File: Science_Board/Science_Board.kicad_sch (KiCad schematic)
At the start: 26 parts, among them J1 Conn_01x02, J10 Conn_01x02, J11 Conn_01x03, J12 Conn_01x03, J13 Conn_01x03, J14 Conn_01x03, J15 Conn_01x03, J16 Conn_01x03, J17 Conn_01x03, J18 Conn_01x03, J19 Conn_01x02, J2 Conn_01x02, J20 Molex_Megafit_02, J5 Conn_01x02, J6 Conn_01x04, J7 Conn_01x03, J8 Conn_01x03, J9 Conn_01x02, U5 PCA9685BS

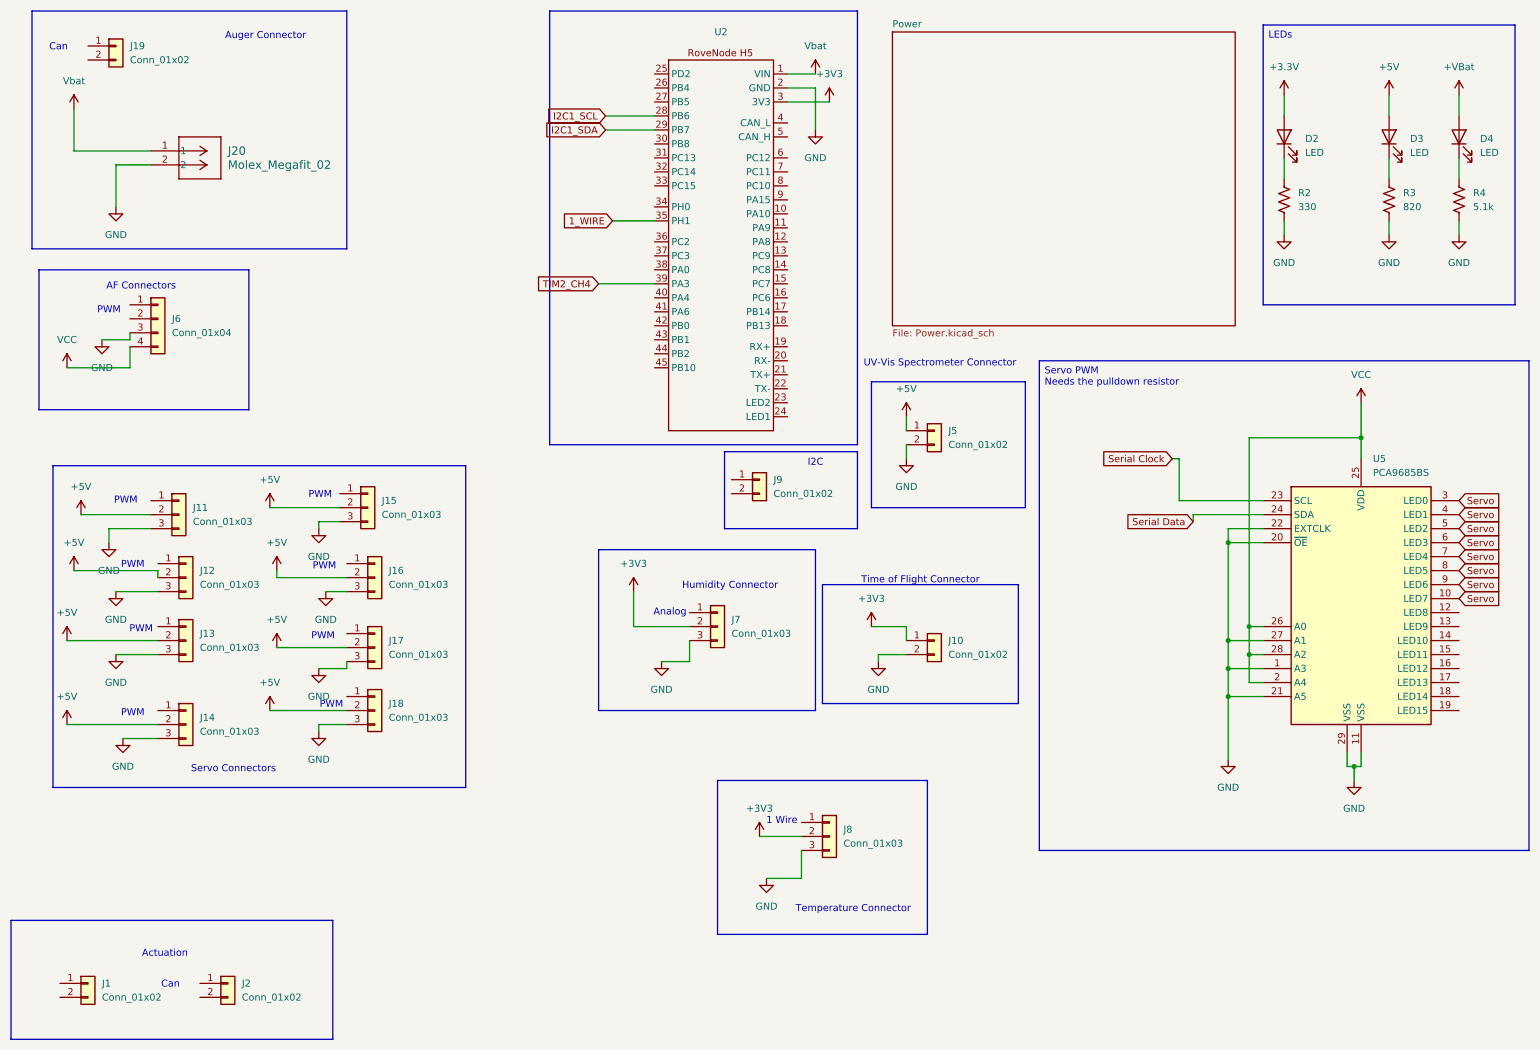
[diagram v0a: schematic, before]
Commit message: connected rovenode the rest of the way better names needed
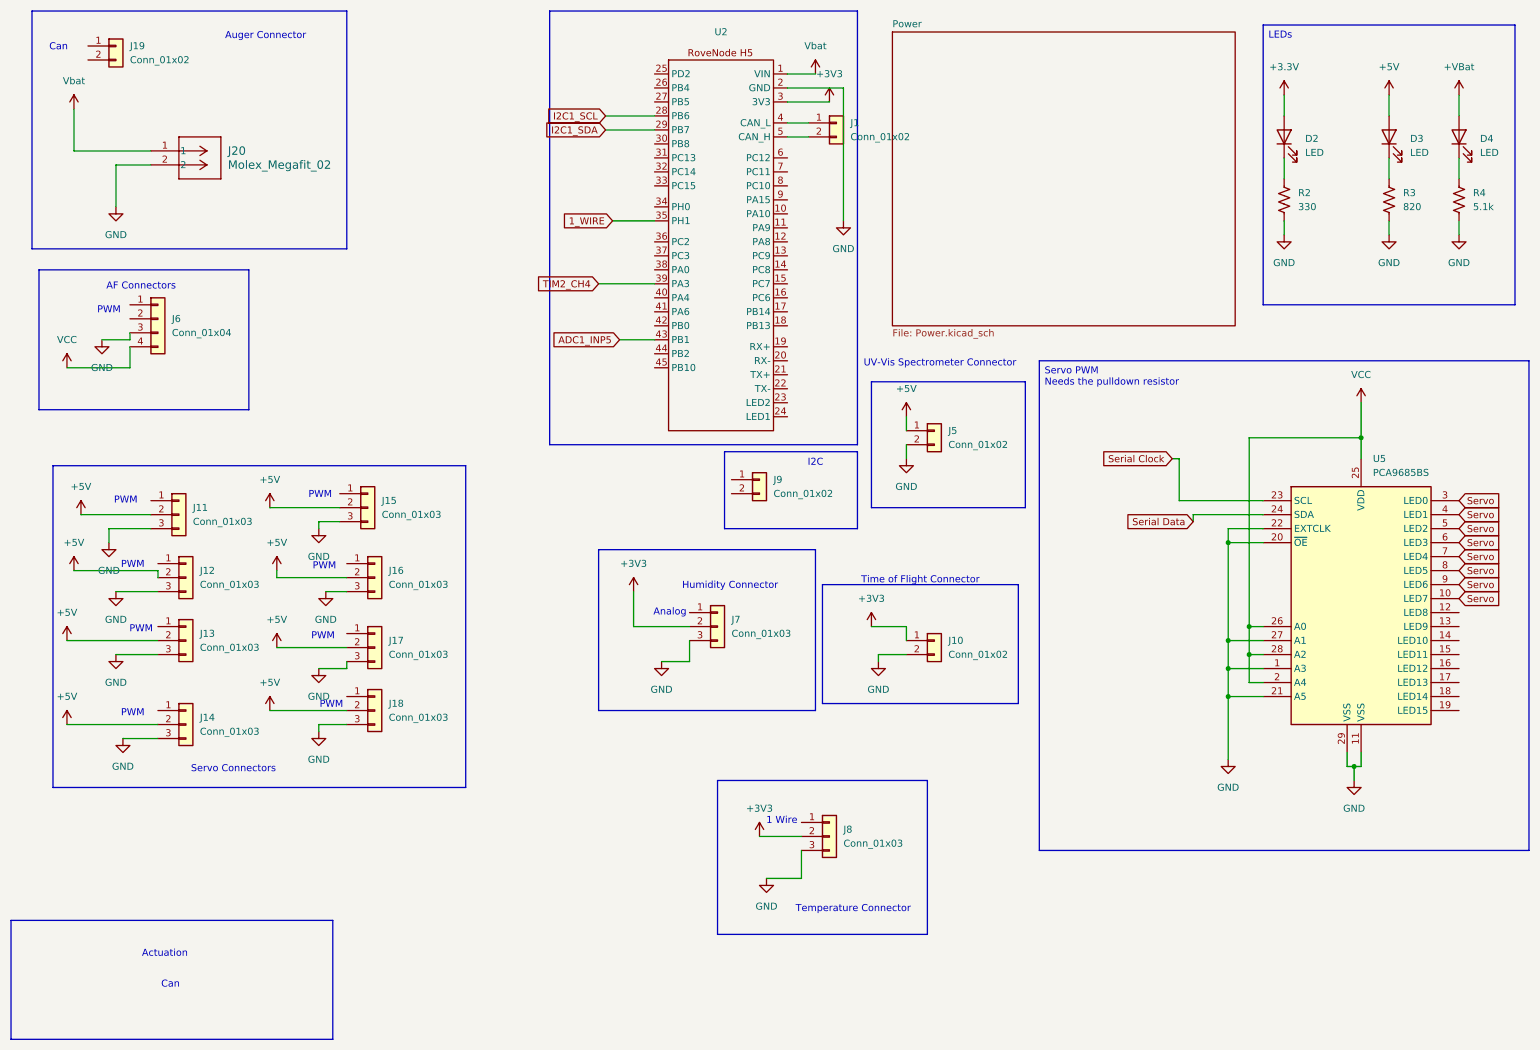
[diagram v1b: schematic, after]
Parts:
- removed J2: Conn_01x02, symbol Connector_Generic:Conn_01x02
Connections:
- net at J1.1 (Pin_1): now also U2.4 (CAN_L)
- net at J1.2 (Pin_2): now also U2.5 (CAN_H)
- net ADC1_INP5: now reaches U2.43 (PB1)
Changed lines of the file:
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@@
 	(wire
 		(pts
+			(xy 153.67 36.83) (xy 149.86 36.83)
+		)
+		(stroke
+			(width 0)
+			(type default)
+		)
+	)
+	(wire
+		(pts
 			(xy 132.08 132.08) (xy 132.08 128.27)
 		)
@@
 	(wire
 		(pts
+			(xy 153.67 34.29) (xy 149.86 34.29)
+		)
+		(stroke
+			(width 0)
+			(type default)
+		)
+	)
+	(wire
+		(pts
 			(xy 259.08 54.61) (xy 259.08 52.07)
 		)
@@
 	(wire
 		(pts
+			(xy 119.38 73.66) (xy 125.73 73.66)
+		)
+		(stroke
+			(width 0)
+			(type default)
+		)
+	)
+	(wire
+		(pts
 			(xy 236.22 107.95) (xy 229.87 107.95)
 		)
@@
 	(wire
 		(pts
-			(xy 154.94 35.56) (xy 154.94 27.94)
+			(xy 160.02 52.07) (xy 160.02 27.94)
 		)
 		(stroke
@@
 	(wire
 		(pts
-			(xy 154.94 27.94) (xy 149.86 27.94)
+			(xy 160.02 27.94) (xy 149.86 27.94)
 		)
 		(stroke
@@
 		)
 	)
+	(global_label "ADC1_INP5"
+		(shape input)
+		(at 119.38 73.66 180)
+		(fields_autoplaced yes)
+		(effects
+			(font
+				(size 1.27 1.27)
+			)
+			(justify right)
+		)
+		(property "Intersheetrefs" "${INTERSHEET_REFS}"
+			(at 106.1743 73.66 0)
+			(hide yes)
+			(show_name no)
+			(do_not_autoplace no)
+			(effects
+				(font
+					(size 1.27 1.27)
+				)
+				(justify right)
+			)
+		)
+	)
 	(global_label "Servo"
 		(shape input)
@@
 	)
 	(symbol
-		(lib_id "Connector_Generic:Conn_01x02")
-		(at 48.26 190.5 0)
-		(unit 1)
-		(body_style 1)
-		(exclude_from_sim no)
-		(in_bom yes)
-		(on_board yes)
-		(in_pos_files yes)
-		(dnp no)
-		(fields_autoplaced yes)
-		(property "Reference" "J2"
-			(at 50.8 190.4999 0)
-			(show_name no)
-			(do_not_autoplace no)
-			(effects
-				(font
-					(size 1.27 1.27)
-				)
-				(justify left)
-			)
-		)
-		(property "Value" "Conn_01x02"
-			(at 50.8 193.0399 0)
-			(show_name no)
-			(do_not_autoplace no)
-			(effects
-				(font
-					(size 1.27 1.27)
-				)
-				(justify left)
-			)
-		)
-		(property "Footprint" ""
-			(at 48.26 190.5 0)
-			(hide yes)
-			(show_name no)
-			(do_not_autoplace no)
-			(effects
-				(font
-					(size 1.27 1.27)
-				)
-			)
-		)
-		(property "Datasheet" ""
-			(at 48.26 190.5 0)
-			(hide yes)
-			(show_name no)
-			(do_not_autoplace no)
-			(effects
-				(font
-					(size 1.27 1.27)
-				)
-			)
-		)
-		(property "Description" "Generic connector, single row, 01x02, script generated (kicad-library-utils/schlib/autogen/connector/)"
-			(at 48.26 190.5 0)
-			(hide yes)
-			(show_name no)
-			(do_not_autoplace no)
-			(effects
-				(font
-					(size 1.27 1.27)
-				)
-			)
-		)
-		(pin "1"
-		)
-		(pin "2"
-		)
-		(instances
-			(project "Science_Board"
-				(path "/4f5c5f7f-4385-4de2-96ca-2ae741ebf691"
-					(reference "J2")
-					(unit 1)
-				)
-			)
-		)
-	)
-	(symbol
 		(lib_id "Connector_Generic:Conn_01x03")
 		(at 137.16 125.73 0)
@@
 	(symbol
 		(lib_id "power:GND")
-		(at 154.94 35.56 0)
+		(at 160.02 52.07 0)
 		(unit 1)
 		(body_style 1)
@@
 		(fields_autoplaced yes)
 		(property "Reference" "#PWR012"
-			(at 154.94 41.91 0)
+			(at 160.02 58.42 0)
 			(hide yes)
 			(show_name no)
@@
 		)
 		(property "Value" "GND"
-			(at 154.94 40.64 0)
+			(at 160.02 57.15 0)
 			(show_name no)
 			(do_not_autoplace no)
@@
 		)
 		(property "Footprint" ""
-			(at 154.94 35.56 0)
+			(at 160.02 52.07 0)
 			(hide yes)
 			(show_name no)
@@
 		)
 		(property "Datasheet" ""
-			(at 154.94 35.56 0)
+			(at 160.02 52.07 0)
 			(hide yes)
 			(show_name no)
@@
 		)
 		(property "Description" "Power symbol creates a global label with name \"GND\" , ground"
-			(at 154.94 35.56 0)
+			(at 160.02 52.07 0)
 			(hide yes)
 			(show_name no)
@@
 	)
 	(symbol
-		(lib_id "Connector_Generic:Conn_01x02")
-		(at 22.86 190.5 0)
-		(unit 1)
-		(body_style 1)
-		(exclude_from_sim no)
-		(in_bom yes)
-		(on_board yes)
-		(in_pos_files yes)
-		(dnp no)
-		(fields_autoplaced yes)
-		(property "Reference" "J1"
-			(at 25.4 190.4999 0)
-			(show_name no)
-			(do_not_autoplace no)
-			(effects
-				(font
-					(size 1.27 1.27)
-				)
-				(justify left)
-			)
-		)
-		(property "Value" "Conn_01x02"
-			(at 25.4 193.0399 0)
-			(show_name no)
-			(do_not_autoplace no)
-			(effects
-				(font
-					(size 1.27 1.27)
-				)
-				(justify left)
-			)
-		)
-		(property "Footprint" ""
-			(at 22.86 190.5 0)
-			(hide yes)
-			(show_name no)
-			(do_not_autoplace no)
-			(effects
-				(font
-					(size 1.27 1.27)
-				)
-			)
-		)
-		(property "Datasheet" ""
-			(at 22.86 190.5 0)
-			(hide yes)
-			(show_name no)
-			(do_not_autoplace no)
-			(effects
-				(font
-					(size 1.27 1.27)
-				)
-			)
-		)
-		(property "Description" "Generic connector, single row, 01x02, script generated (kicad-library-utils/schlib/autogen/connector/)"
-			(at 22.86 190.5 0)
-			(hide yes)
-			(show_name no)
-			(do_not_autoplace no)
-			(effects
-				(font
-					(size 1.27 1.27)
-				)
-			)
-		)
-		(pin "1"
-		)
-		(pin "2"
-		)
-		(instances
-			(project "Science_Board"
-				(path "/4f5c5f7f-4385-4de2-96ca-2ae741ebf691"
-					(reference "J1")
-					(unit 1)
-				)
-			)
-		)
-	)
-	(symbol
 		(lib_id "power:GND")
 		(at 259.08 54.61 0)
@@
 					(unit 1)
 				)
+			)
+		)
+	)
+	(symbol
+		(lib_id "Connector_Generic:Conn_01x02")
+		(at 158.75 34.29 0)
+		(unit 1)
+		(body_style 1)
+		(exclude_from_sim no)
+		(in_bom yes)
+		(on_board yes)
+		(in_pos_files yes)
+		(dnp no)
+		(fields_autoplaced yes)
+		(property "Reference" "J1"
+			(at 161.29 34.2899 0)
+			(show_name no)
+			(do_not_autoplace no)
+			(effects
+				(font
+					(size 1.27 1.27)
+				)
+				(justify left)
+			)
+		)
+		(property "Value" "Conn_01x02"
+			(at 161.29 36.8299 0)
+			(show_name no)
+			(do_not_autoplace no)
+			(effects
+				(font
+					(size 1.27 1.27)
+				)
+				(justify left)
+			)
+		)
+		(property "Footprint" ""
+			(at 158.75 34.29 0)
+			(hide yes)
+			(show_name no)
+			(do_not_autoplace no)
+			(effects
+				(font
+					(size 1.27 1.27)
+				)
+			)
+		)
+		(property "Datasheet" ""
+			(at 158.75 34.29 0)
+			(hide yes)
+			(show_name no)
+			(do_not_autoplace no)
+			(effects
+				(font
+					(size 1.27 1.27)
+				)
+			)
+		)
+		(property "Description" "Generic connector, single row, 01x02, script generated (kicad-library-utils/schlib/autogen/connector/)"
+			(at 158.75 34.29 0)
+			(hide yes)
+			(show_name no)
+			(do_not_autoplace no)
+			(effects
+				(font
+					(size 1.27 1.27)
+				)
+			)
+		)
+		(pin "1"
+		)
+		(pin "2"
+		)
+		(instances
+			(project "Science_Board"
+				(path "/4f5c5f7f-4385-4de2-96ca-2ae741ebf691"
+					(reference "J1")
+					(unit 1)
+				)

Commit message: Hooked up a lot of connections
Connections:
- net TIM2_CH4 is gone; now on net PWM_TIM2_CH4: U2.39 (PA3)
- net 1_WIRE: now also J8.1 (Pin_1)
- net ADC1_INP5: now also J7.1 (Pin_1)
- net I2C1_SCL: now also J9.1 (Pin_1)
- net I2C1_SDA: now also J9.2 (Pin_2)
- net Servo2: now reaches J12.1 (Pin_1)
- net Servo2: now also U5.5 (LED2)
- net Servo1: now reaches J15.1 (Pin_1)
- net Servo1: now also U5.4 (LED1)
- net CANH: now reaches J19.1 (Pin_1)
- net CANH: now also J1.1 (Pin_1)
- net CANL: now reaches J19.2 (Pin_2)
- net CANL: now also J1.2 (Pin_2)
- net Servo4: now reaches J13.1 (Pin_1)
- net Servo4: now also U5.7 (LED4)
- net Servo5: now reaches J17.1 (Pin_1)
- net Servo5: now also U5.8 (LED5)
- net PWM_TIM2_CH1: now reaches J6.1 (Pin_1)
- net PWM_TIM2_CH1: now also U2.38 (PA0)
- net PWM_TIM2_CH4: now reaches J6.2 (Pin_2)
- net Servo3: now reaches J16.1 (Pin_1)
- net Servo3: now also U5.6 (LED3)
- net Servo0: now reaches J11.1 (Pin_1)
- net Servo0: now also U5.3 (LED0)
- net at U2.4 (CAN_L): no longer J1.1 (Pin_1)
- net at U2.5 (CAN_H): no longer J1.2 (Pin_2)
- net Servo6: now reaches J14.1 (Pin_1)
- net Servo6: now also U5.9 (LED6)
- net Servo7: now reaches J18.1 (Pin_1)
- net Servo7: now also U5.10 (LED7)
- removed net Servo: U5.10 (LED7), U5.3 (LED0), U5.4 (LED1), U5.5 (LED2), U5.6 (LED3), U5.7 (LED4), U5.8 (LED5), U5.9 (LED6)
- no-connect marks 0 -> 38
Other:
- note removed: "1 Wire"
- note removed: "Analog"
- note removed: "PWM"
- moved on the sheet: J13, J14, J18

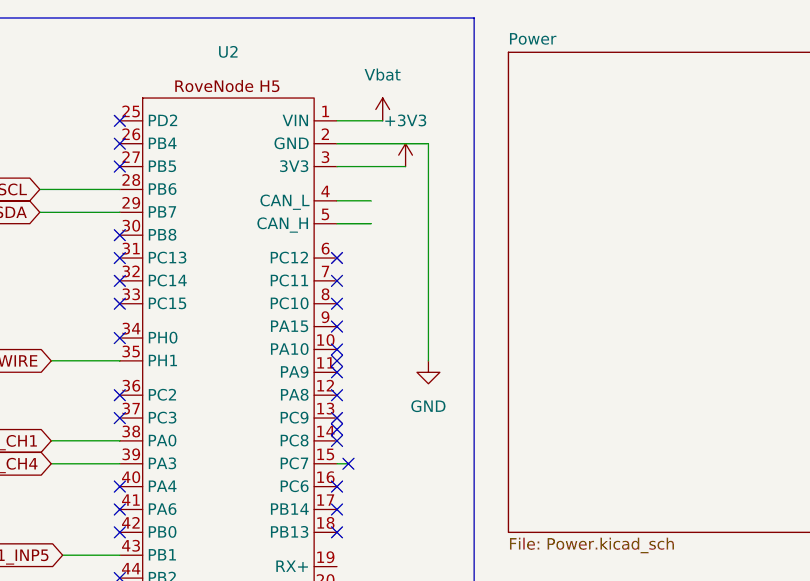
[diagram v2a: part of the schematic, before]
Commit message: connected can h and can l to points
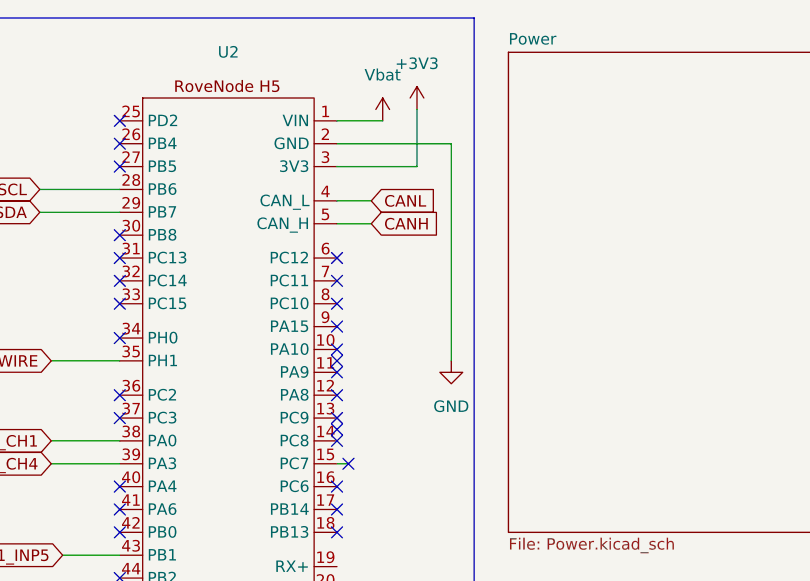
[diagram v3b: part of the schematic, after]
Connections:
- net CANH: now also U2.5 (CAN_H)
- net CANL: now also U2.4 (CAN_L)
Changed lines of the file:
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@@
 	(wire
 		(pts
+			(xy 158.75 30.48) (xy 149.86 30.48)
+		)
+		(stroke
+			(width 0)
+			(type default)
+		)
+	)
+	(wire
+		(pts
 			(xy 144.78 157.48) (xy 144.78 163.83)
 		)
@@
 	(wire
 		(pts
+			(xy 158.75 24.13) (xy 158.75 30.48)
+		)
+		(stroke
+			(width 0)
+			(type default)
+		)
+	)
+	(wire
+		(pts
 			(xy 20.32 39.37) (xy 34.29 39.37)
 		)
@@
 	(wire
 		(pts
-			(xy 149.86 30.48) (xy 157.48 30.48)
-		)
-		(stroke
-			(width 0)
-			(type default)
-		)
-	)
-	(wire
-		(pts
 			(xy 171.45 95.25) (xy 171.45 92.71)
 		)
@@
 	(wire
 		(pts
-			(xy 160.02 52.07) (xy 160.02 27.94)
+			(xy 162.56 52.07) (xy 162.56 27.94)
 		)
 		(stroke
@@
 	(wire
 		(pts
-			(xy 160.02 27.94) (xy 149.86 27.94)
+			(xy 162.56 27.94) (xy 149.86 27.94)
 		)
 		(stroke
@@
 		)
 	)
+	(global_label "CANH"
+		(shape input)
+		(at 153.67 36.83 0)
+		(fields_autoplaced yes)
+		(effects
+			(font
+				(size 1.27 1.27)
+			)
+			(justify left)
+		)
+		(property "Intersheetrefs" "${INTERSHEET_REFS}"
+			(at 161.6748 36.83 0)
+			(hide yes)
+			(show_name no)
+			(do_not_autoplace no)
+			(effects
+				(font
+					(size 1.27 1.27)
+				)
+				(justify left)
+			)
+		)
+	)
+	(global_label "CANL"
+		(shape input)
+		(at 153.67 34.29 0)
+		(fields_autoplaced yes)
+		(effects
+			(font
+				(size 1.27 1.27)
+			)
+			(justify left)
+		)
+		(property "Intersheetrefs" "${INTERSHEET_REFS}"
+			(at 161.3724 34.29 0)
+			(hide yes)
+			(show_name no)
+			(do_not_autoplace no)
+			(effects
+				(font
+					(size 1.27 1.27)
+				)
+				(justify left)
+			)
+		)
+	)
 	(global_label "Servo6"
 		(shape input)
@@
 	(symbol
 		(lib_id "power:VCC")
-		(at 157.48 30.48 0)
+		(at 158.75 24.13 0)
 		(unit 1)
 		(body_style 1)
@@
 		(fields_autoplaced yes)
 		(property "Reference" "#PWR013"
-			(at 157.48 34.29 0)
+			(at 158.75 27.94 0)
 			(hide yes)
 			(show_name no)
@@
 		)
 		(property "Value" "+3V3"
-			(at 157.48 25.4 0)
+			(at 158.75 19.05 0)
 			(show_name no)
 			(do_not_autoplace no)
@@
 		)
 		(property "Footprint" "Package_QFP:TQFP-44_10x10mm_P0.8mm"
-			(at 157.48 30.48 0)
+			(at 158.75 24.13 0)
 			(hide yes)
 			(show_name no)
@@
 		)
 		(property "Datasheet" ""
-			(at 157.48 30.48 0)
+			(at 158.75 24.13 0)
 			(hide yes)
 			(show_name no)
@@
 		)
 		(property "Description" "Power symbol creates a global label with name \"VCC\""
-			(at 157.48 30.48 0)
+			(at 158.75 24.13 0)
 			(hide yes)
 			(show_name no)
@@
 	(symbol
 		(lib_id "power:GND")
-		(at 160.02 52.07 0)
+		(at 162.56 52.07 0)
 		(unit 1)
 		(body_style 1)
@@
 		(fields_autoplaced yes)
 		(property "Reference" "#PWR012"
-			(at 160.02 58.42 0)
+			(at 162.56 58.42 0)
 			(hide yes)
 			(show_name no)
@@
 		)
 		(property "Value" "GND"
-			(at 160.02 57.15 0)
+			(at 162.56 57.15 0)
 			(show_name no)
 			(do_not_autoplace no)
@@
 		)
 		(property "Footprint" ""
-			(at 160.02 52.07 0)
+			(at 162.56 52.07 0)
 			(hide yes)
 			(show_name no)
@@
 		)
 		(property "Datasheet" ""
-			(at 160.02 52.07 0)
+			(at 162.56 52.07 0)
 			(hide yes)
 			(show_name no)
@@
 		)
 		(property "Description" "Power symbol creates a global label with name \"GND\" , ground"
-			(at 160.02 52.07 0)
+			(at 162.56 52.07 0)
 			(hide yes)
 			(show_name no)
